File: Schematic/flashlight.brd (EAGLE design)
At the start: 33.2 x 17.8 mm, 2 parts, among them IC1 AMC7135SOT-89

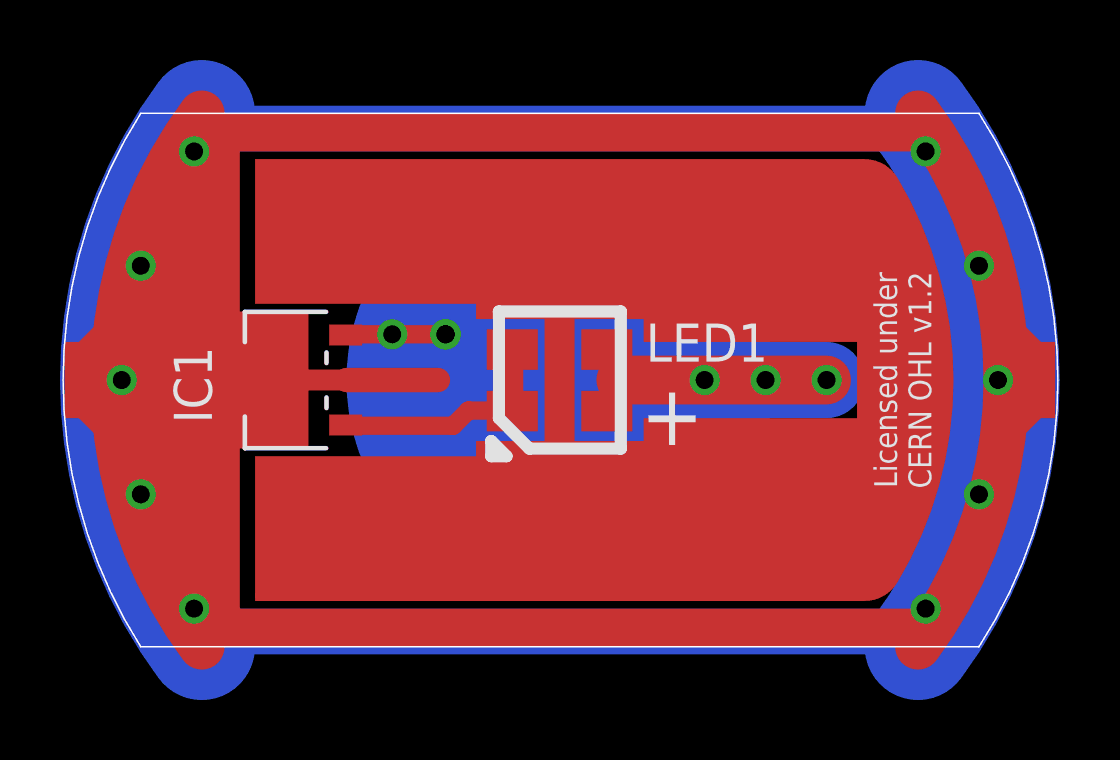
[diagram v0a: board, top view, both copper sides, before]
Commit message: Start revision 3.3 by adding a protection diode.
* Add a protection diode for the current regulator.
* Adjust the footprint of the switch to make it slightly easier
  to position and solder.
* Add text for the Diode to the documentation; however it should
  have updated pictures for the board throughout since this is
  more than a cosmetic change.
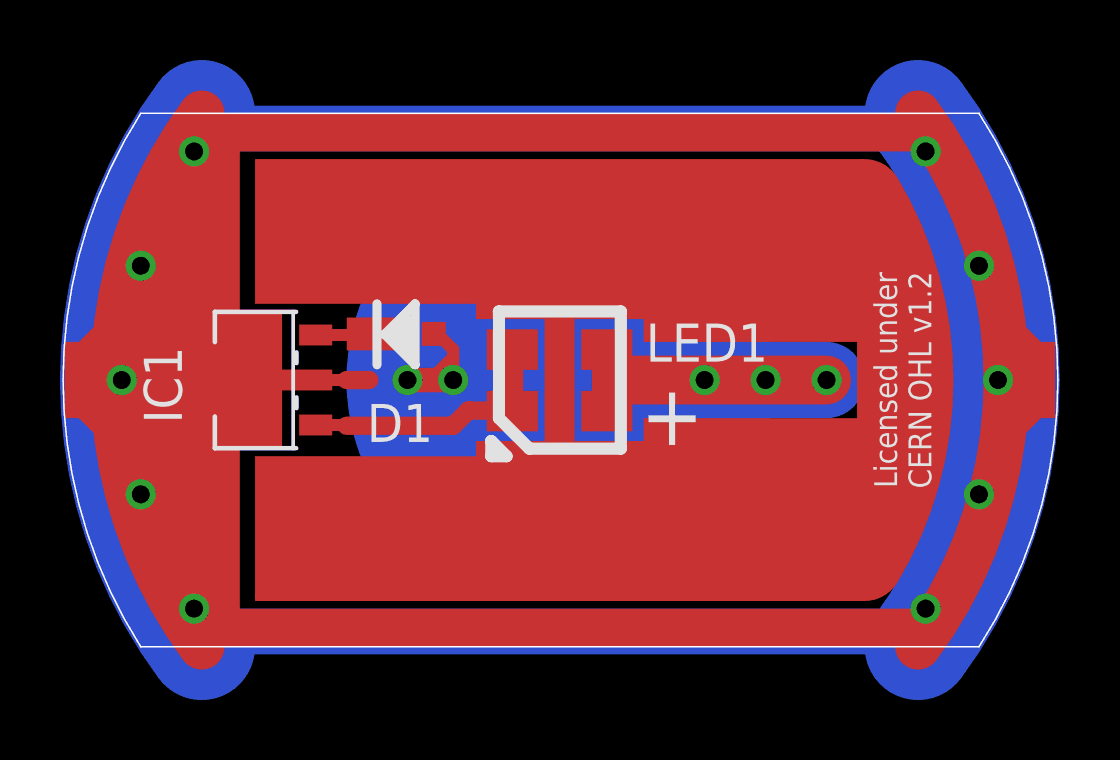
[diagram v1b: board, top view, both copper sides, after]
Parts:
- added D1: (no value), chrisy-components:DIODE323
- moved IC1 1.00 mm to (6.62, 8.89)
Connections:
- new net N$25: D1.C, IC1.1
- net N$28: no longer IC1.1
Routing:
- net N$29: track 23.5 -> 10.9 mm, vias 4 -> 2
- net N$28: track 6.83 -> 0.00 mm, vias 1 -> 0
- net N$26: track 0.00 -> 4.34 mm, vias 0 -> 2
- net N$25: track 0.00 -> 2.08 mm
- net N$27: track 0.00 -> 2.03 mm
- net N$30: track 3.05 -> 1.78 mm
- net N$3: track 5.76 -> 6.76 mm
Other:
- board text added: "Top Board Rev. 3.3"
- board text removed: "Top Board Rev. 3.2"
